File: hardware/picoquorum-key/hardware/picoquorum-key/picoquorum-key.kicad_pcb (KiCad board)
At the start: 2 copper layers, 50 x 53 mm, 69 parts, among them J1 USB-C, J2 ST7789 1.14in panel, J3 USB-C plug, straddle, Q1 AO3401A, Q2 MMBT3904, SW1 D0 Reject, SW2 D1 Next, SW3 D2 Sign, SW6 BOOT, SW7 RESET, U1 ESP32-S3-WROOM-1-N8R2, U2 ATECC608C-MAHDA, U3 AMS1117-3.3, U4 USBLC6-2SC6, U5 AP22653W6-7, U6 USBLC6-2SC6, U7 USBLC6-2SC6

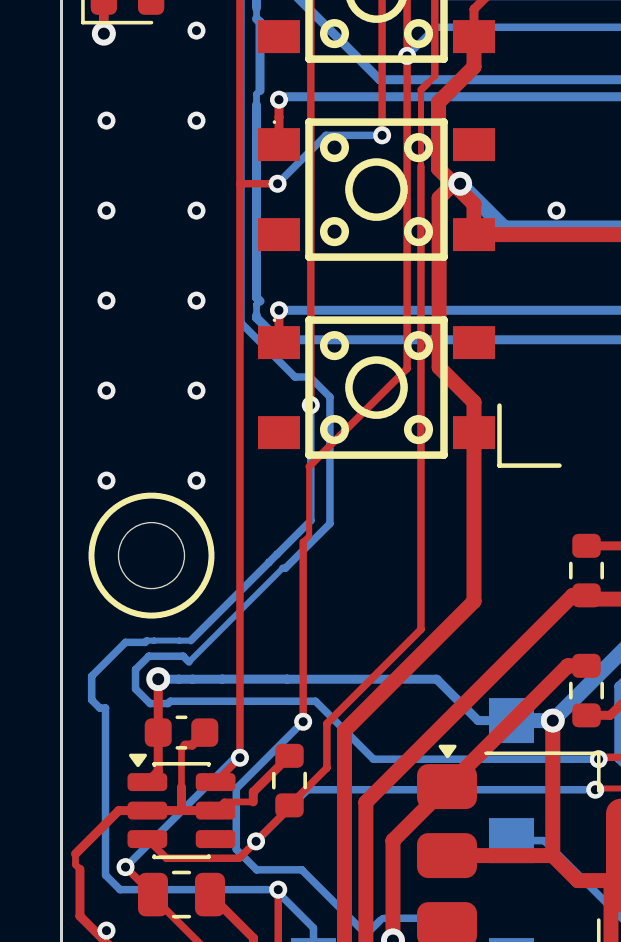
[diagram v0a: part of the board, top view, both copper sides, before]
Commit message: picoquorum-key rev B: D5, a Schottky between U5 and the plug
U5 (AP22653) blocks reverse current only while off; on, it limits it
to 0.32 A, which would push 3V3 past the S3's 3.6 V if 5 V reached the
plug's VBUS. D5 (1N5819WS, C191023, basic) now sits between U5's output
(new net VKEY_SW) and VKEY: 5 V on the plug stops there, U5 on or off.
About 0.2 V of drop at the key's current, so the key sees ~3.1 V.

- R19/R20 move to VKEY_SW: a key that is off still isn't fed through
  its bus, and 5 V on the plug no longer reaches GPIO38/39's clamps.
- R23 (10k) drains VKEY, which U5's discharge can't reach through D5.
- Board: D5 and R23 in VKEY's run up the left strip (4, 19.5) and
  (2.2, 19.5); the track was cut for D5, four ground stitching vias
  made room, R23's ground pad has its own via. Nothing else moved.
- PINS.md drops the GPIO38/39 check before enabling: it is not needed.
- test_key_port: nothing on VKEY leads to 3V3 or VKEY_SW but D5.
  test_spice and the twin follow the pull-ups to VKEY_SW.
- DESIGN.md: why not U5 alone, the AP22653A or the TPS22917 (its
  blocking needs 0.5 A of reverse current first). Open: the ATECC608C's
  pin limit, with the bus at 3.3 V and the key at ~3.1 V.

ERC 0, DRC 0 with schematic parity. Port BOM/CPL gain D5 and R23; the
base BOM is unchanged. tools/test.sh: 162 tests, one failure, test_3d's
J3 without a model, as before. Approved pictures remade (KiCad 10.0.6).

Co-Authored-By: Claude Opus 5.5 <noreply@anthropic.com>
Claude-Session: https://claude.ai/code/session_015Mrfds5ggPmPXMnhiEk5Pk
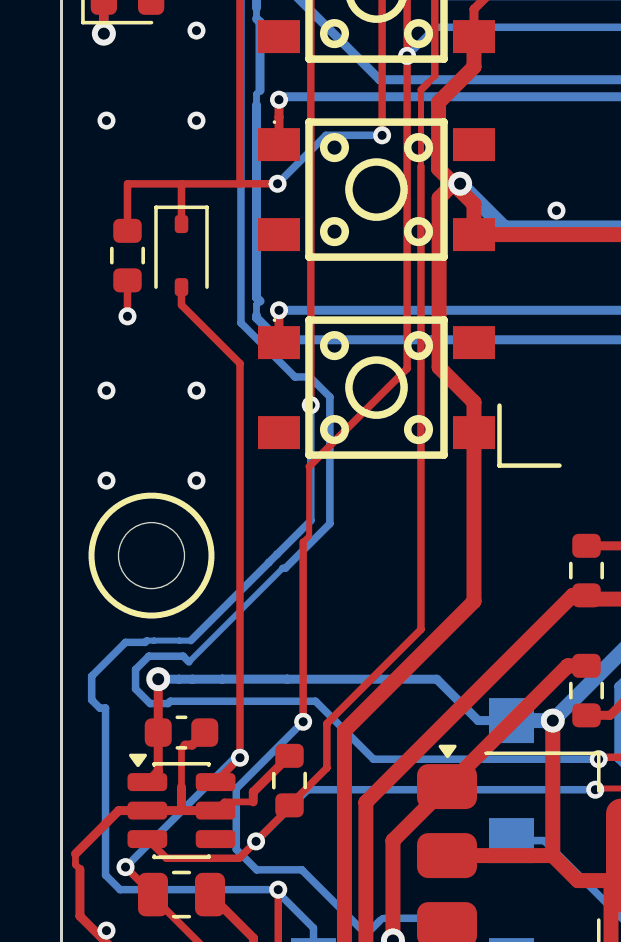
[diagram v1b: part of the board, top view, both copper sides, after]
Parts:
- added D5: 1N5819WS, Diode_SMD:D_SOD-323, F.Cu at (104.0, 79.5)
- added R23: 10k, Resistor_SMD:R_0603_1608Metric, F.Cu at (102.2, 79.5)
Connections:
- C10 pad 1: VKEY -> VKEY_SW
- R19 pad 1: VKEY -> VKEY_SW
- R20 pad 1: VKEY -> VKEY_SW
- U5 pad 6: VKEY -> VKEY_SW
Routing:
- net VKEY_SW: track 0.00 -> 29.7 mm, vias 0 -> 2
- net VKEY: track 78.3 -> 52.6 mm, vias 6 -> 4
- net GND: track 368.0 -> 369.2 mm, vias 65 -> 62
